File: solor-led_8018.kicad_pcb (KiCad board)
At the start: 2 copper layers, 51.4 x 12.7 mm, 6 parts, among them J1 Solar, J2 XY8018

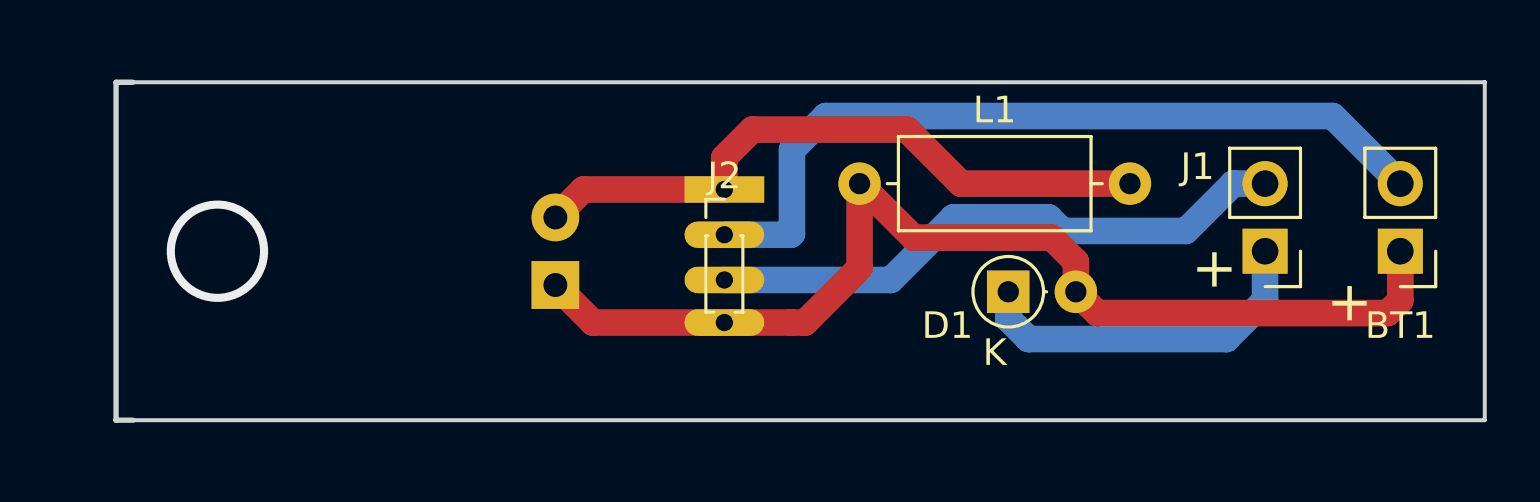
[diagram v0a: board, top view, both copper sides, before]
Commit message: add screw point
add screw point
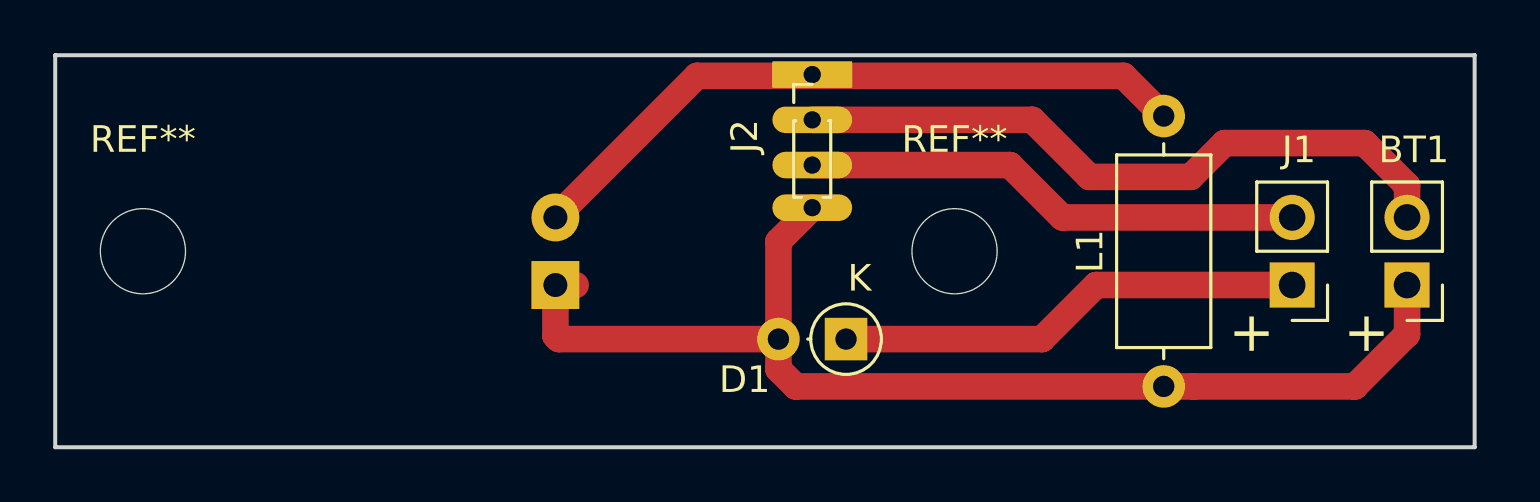
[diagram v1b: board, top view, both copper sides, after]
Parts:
- added REF**: MountingHole_3.2mm_M3, MountingHole:MountingHole_3.2mm_M3, F.Cu at (149.6, 100.3)
- added REF**: MountingHole_3.2mm_M3, MountingHole:MountingHole_3.2mm_M3, F.Cu at (119.1, 100.3)
- moved L1 13.7 mm to (157.5, 105.4), turned to 90 degrees
- moved D1 6.35 mm to (145.5, 103.6), turned to 180 degrees
- moved J2 5.44 mm to (144.3, 94.7)
- moved J1 1.63 mm to (162.3, 101.6)
- moved BT1 1.30 mm to (166.6, 101.6)
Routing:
- net GND: track 30.1 -> 25.6 mm
- net Net-(D1-Pad1): track 13.4 -> 17.6 mm
- net Net-(J1-Pad2): track 22.2 -> 18.8 mm
- net Net-(BT1-Pad1): track 41.1 -> 44.2 mm
- net Net-(D2-Pad2): track 24.5 -> 25.7 mm
- net (no net): vias 1 -> 0
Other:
- board size 51.4 x 12.7 mm -> 53.3 x 14.7 mm
- board text added: "GeeTsuku"
